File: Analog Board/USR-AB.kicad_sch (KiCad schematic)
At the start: 3 parts, among them U2 CD74HC4067SM96, U3 SC0918

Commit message: updated PDB and analog board
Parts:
- added J2, J3: S5B-XH-A_LF__SN_, USR:JST-XH 5-PIN, symbol USR:JST-XH (5-pin_RA)
- added U1: ~, USR:JST-XA 4-PIN, symbol USR:JST-XA 4-PIN
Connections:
- net LOADCELL_1 is gone; now on net M1_THERM: U2.5 (I4)
- net LOADCELL_2 is gone; now on net M2_THERM: U2.4 (I5)
- net LOADCELL_3 is gone; now on net M3_THERM: U2.3 (I6)
- net LOADCELL_4 is gone; now on net M4_THERM: U2.2 (I7)
- net AMB_THERM: now also U2.21 (I10), J2.5; no longer U2.17 (I14)
- net DRIVE1_HE: now also J1.32 (DRIVE1_HE), U2.23 (I8); no longer U2.19 (I12)
- net DRIVE2_HE: now also J1.33 (DRIVE2_HE), U2.22 (I9); no longer U2.18 (I13)
- net GND: now also U3.33 (AGND)
- net M1_THERM: now also J2.1; no longer U2.23 (I8)
- net M2_THERM: now also J2.2; no longer U2.22 (I9)
- net M3_THERM: now also J2.3; no longer U2.21 (I10)
- net M4_THERM: now also J2.4; no longer U2.20 (I11)
- net UART_RX: no longer U3.17 (GP13)
- net UART_TX: no longer U3.16 (GP12)
- net Connection_5: now reaches U2.16 (I15)
- net Connection_5: now also J3.5
- new net CLK: U1.3
- new net CS: U1.4
- new net Connection_1: J3.1, U2.20 (I11)
- new net Connection_2: J3.2, U2.19 (I12)
- new net Connection_3: J3.3, U2.18 (I13)
- new net Connection_4: J3.4, U2.17 (I14)
- new net Din: U1.1
- new net Dout: U1.2
- new net UART_RX-(host): U3.16 (GP12)
- new net UART_TX-(host): U3.17 (GP13)
- no-connect marks 3 -> 1
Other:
- note added: "(Look at PICO pinout for what these mean) SPIO SCK: CLK SPIO TX: Din SPIO RX: Dout SPIO CSn: CS"
- note added: "PDB HE sensors"
- note added: "Unused MUX connections"
- note removed: "Questions: - What analog inputs are coming in - where do we want the pico connected? - what connections on the backplane pinnout correspond to the pico on the analog board? - Pico (analog) is just connected to the UART connection on the backplane"
- note removed: "analog inputs: - load cell - load cell - load cell - load cell - LA feedback - LA feedback - LA feedback - HE sensor (PDB) - HE sensor (PDB) ... - What else?"
- note removed: "look into the analog ground for the chip"
- note removed: "use the same pin numbers for the multiplexer pins on the sheet"

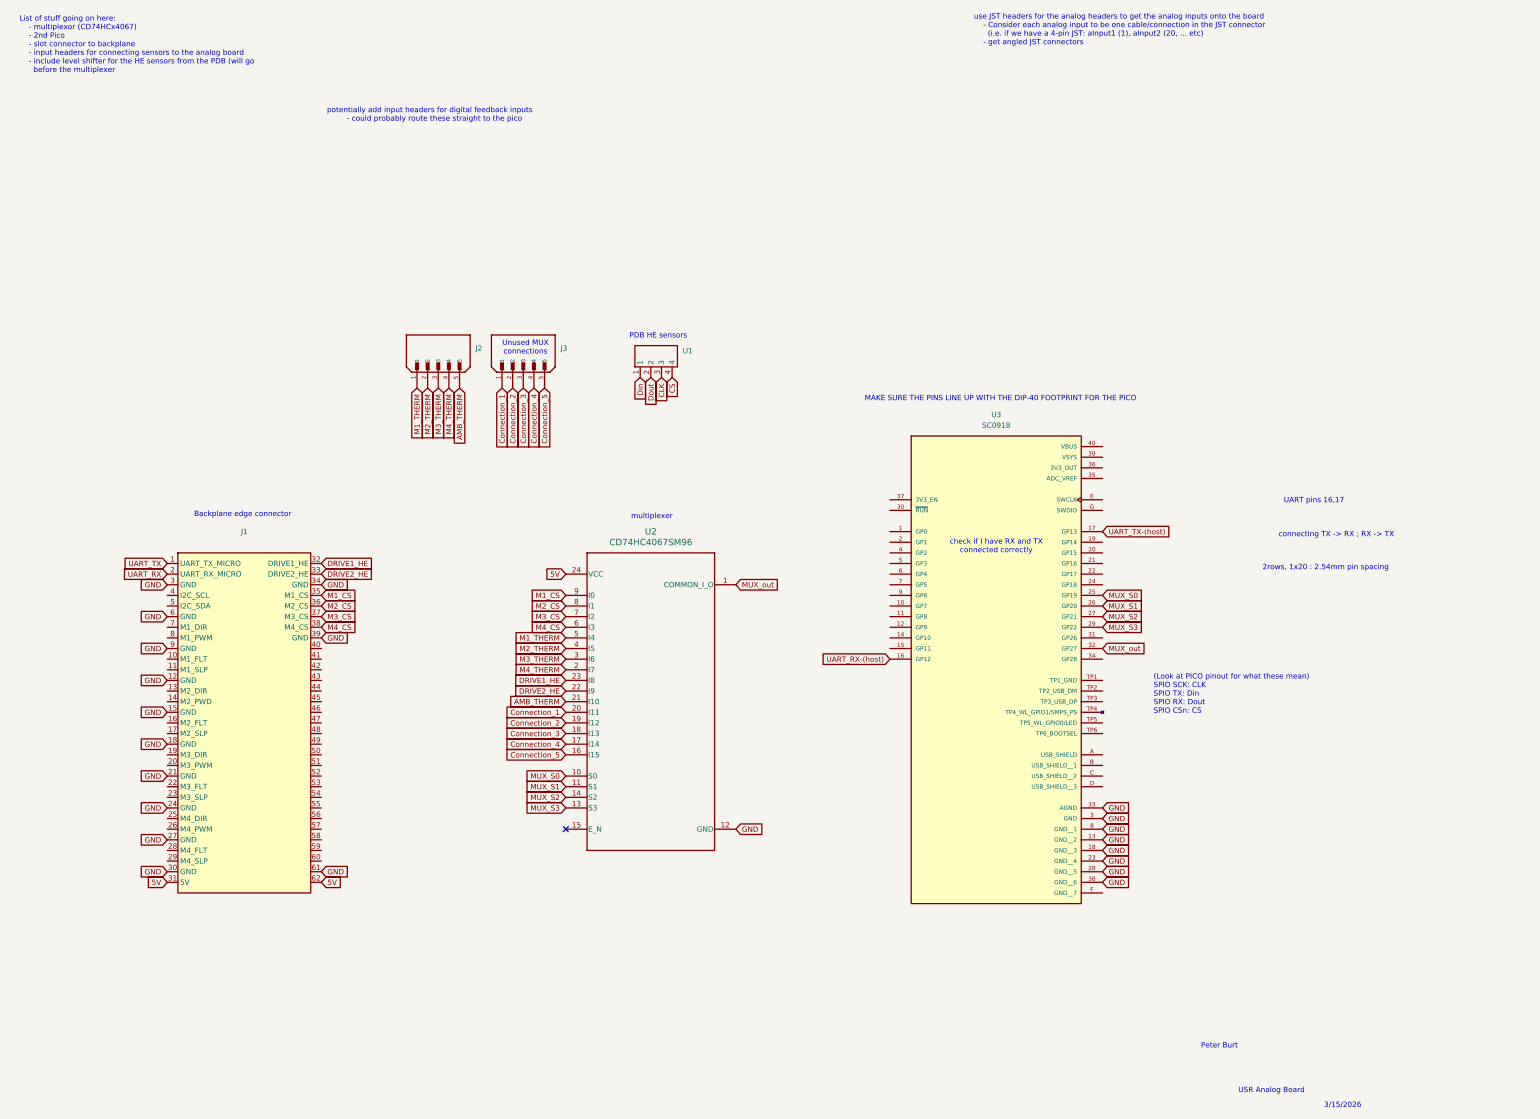
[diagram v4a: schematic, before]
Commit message: Updated analog board connections
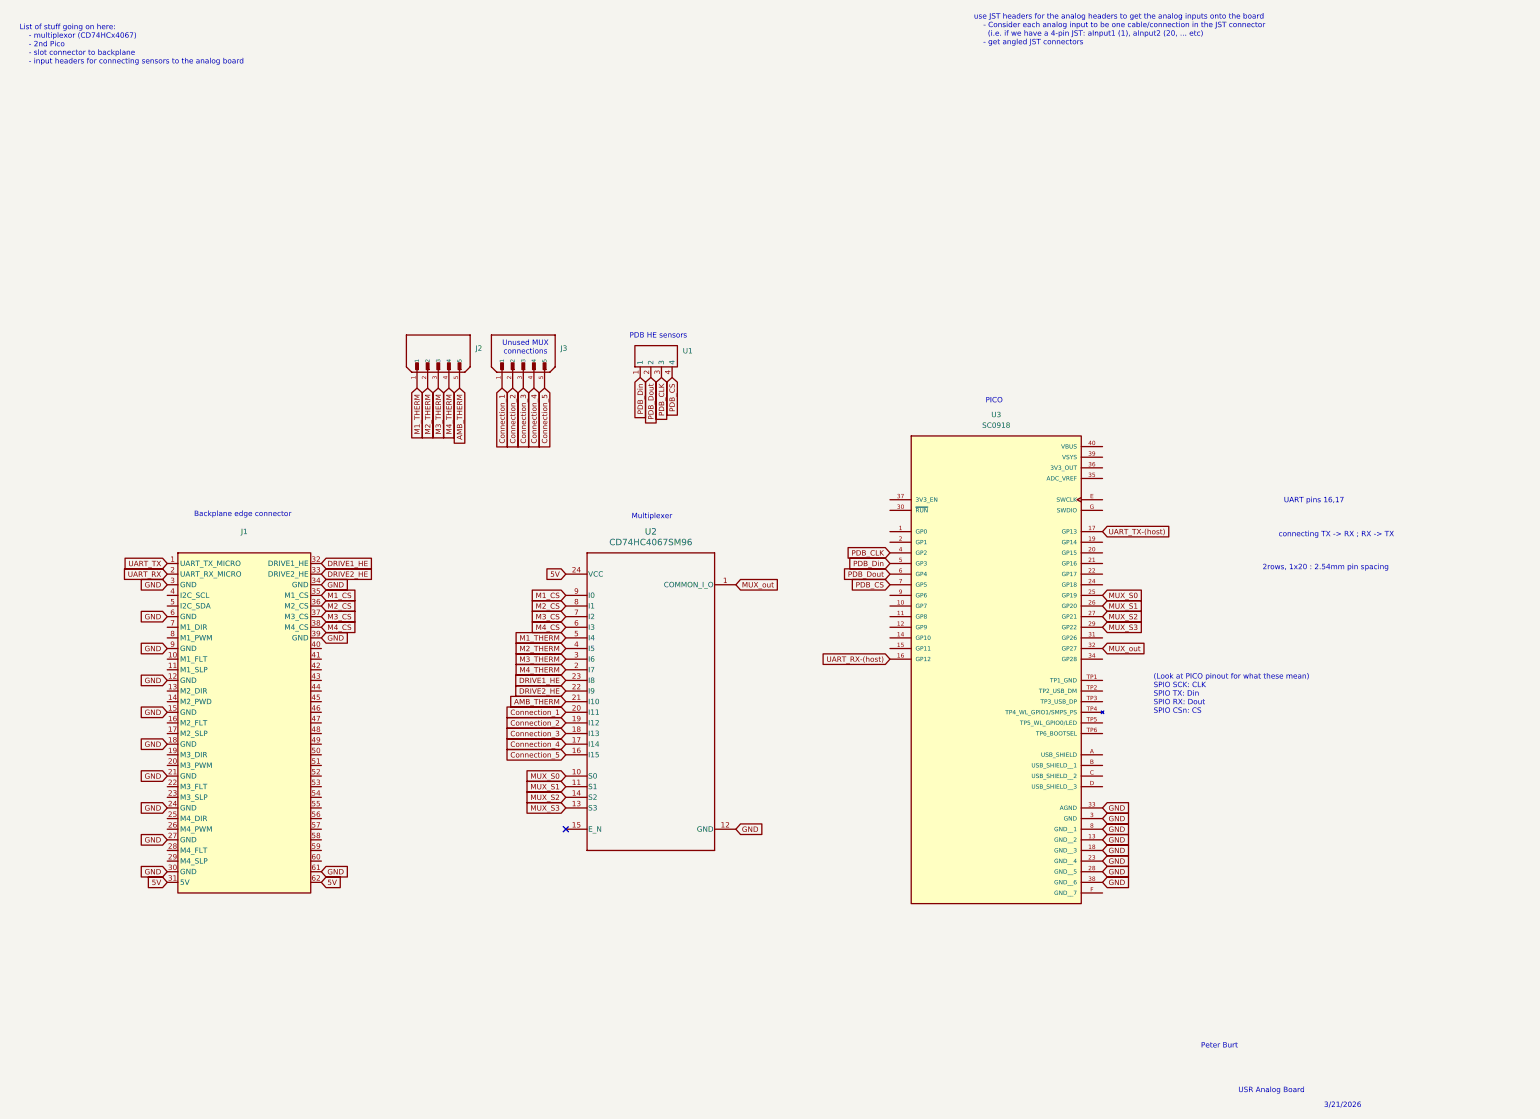
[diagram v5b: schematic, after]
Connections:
- net CLK is gone; now on net PDB_CLK: U1.3
- net CS is gone; now on net PDB_CS: U1.4
- net Din is gone; now on net PDB_Din: U1.1
- net Dout is gone; now on net PDB_Dout: U1.2
- net PDB_CLK: now reaches U3.4 (GP2)
- net PDB_Din: now reaches U3.5 (GP3)
- net PDB_Dout: now reaches U3.6 (GP4)
- net PDB_CS: now reaches U3.7 (GP5)
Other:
- note added: "3/21/2026"
- note added: "List of stuff going on here: - multiplexor (CD74HCx4067) - 2nd Pico - slot connector to backplane - input headers for connecting sensors to the analog board"
- note added: "Multiplexer"
- note added: "PICO"
- note removed: "3/15/2026"
- note removed: "List of stuff going on here: - multiplexor (CD74HCx4067) - 2nd Pico - slot connector to backplane - input headers for connecting sensors to the analog board - include level shifter for the HE sensors from the PDB (will go before the multiplexer"
- note removed: "MAKE SURE THE PINS LINE UP WITH THE DIP-40 FOOTPRINT FOR THE PICO"
- note removed: "check if I have RX and TX connected correctly"
- note removed: "multiplexer"
- note removed: "potentially add input headers for digital feedback inputs - could probably route these straight to the pico"
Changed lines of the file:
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@@
+		)
+	)
+	(text "PICO"
+		(exclude_from_sim no)
+		(at 252.222 112.268 0)
+		(effects
+			(font
+				(size 1.27 1.27)
+			)
 		)
 	)
@@
 		)
 	)
-	(text "List of stuff going on here:\n	- multiplexor (CD74HCx4067)	\n	- 2nd Pico\n	- slot connector to backplane	\n	- input headers for connecting sensors to the analog board\n	- include level shifter for the HE sensors from the PDB (will go \n	  before the multiplexer"
+	(text "List of stuff going on here:\n	- multiplexor (CD74HCx4067)	\n	- 2nd Pico\n	- slot connector to backplane	\n	- input headers for connecting sensors to the analog board"
 		(exclude_from_sim no)
 		(at 19.304 27.178 0)
@@
 		)
 	)
-	(text "potentially add input headers for digital feedback inputs \n	- could probably route these straight to the pico"
-		(exclude_from_sim no)
-		(at 117.348 43.942 0)
-		(effects
-			(font
-				(size 1.27 1.27)
-			)
-		)
-	)
 	(text "Unused MUX \nconnections"
 		(exclude_from_sim no)
@@
 		)
 	)
-	(text "3/15/2026"
+	(text "3/21/2026"
 		(exclude_from_sim no)
 		(at 335.534 280.67 0)
@@
 		)
 	)
-	(text "check if I have RX and TX\nconnected correctly"
-		(exclude_from_sim no)
-		(at 252.73 147.066 0)
-		(effects
-			(font
-				(size 1.27 1.27)
-			)
-		)
-	)
-	(text "multiplexer\n"
+	(text "Multiplexer\n"
 		(exclude_from_sim no)
 		(at 170.434 139.954 0)
@@
 		)
 	)
-	(text "MAKE SURE THE PINS LINE UP WITH THE DIP-40 FOOTPRINT FOR THE PICO"
-		(exclude_from_sim no)
-		(at 253.746 111.76 0)
-		(effects
-			(font
-				(size 1.27 1.27)
-			)
-		)
-	)
 	(no_connect
 		(at 149.86 214.63)
@@
 		)
 	)
+	(global_label "PDB_Dout"
+		(shape input)
+		(at 227.33 153.67 180)
+		(fields_autoplaced yes)
+		(effects
+			(font
+				(size 1.27 1.27)
+			)
+			(justify right)
+		)
+		(property "Intersheetrefs" "${INTERSHEET_REFS}"
+			(at 215.2735 153.67 0)
+			(effects
+				(font
+					(size 1.27 1.27)
+				)
+				(justify right)
+				(hide yes)
+			)
+		)
+	)
 	(global_label "MUX_S1"
 		(shape input)
@@
 		)
 	)
-	(global_label "Din"
+	(global_label "PDB_Din"
 		(shape input)
 		(at 167.64 106.68 270)
@@
 		)
 		(property "Intersheetrefs" "${INTERSHEET_REFS}"
-			(at 167.64 112.689 90)
+			(at 167.64 117.4666 90)
 			(effects
 				(font
@@
 		)
 	)
-	(global_label "CLK"
+	(global_label "PDB_CLK"
 		(shape input)
 		(at 172.72 106.68 270)
@@
 		)
 		(property "Intersheetrefs" "${INTERSHEET_REFS}"
-			(at 172.72 113.2333 90)
+			(at 172.72 118.0109 90)
 			(effects
 				(font
@@
 		)
 	)
+	(global_label "PDB_CLK"
+		(shape input)
+		(at 227.33 148.59 180)
+		(fields_autoplaced yes)
+		(effects
+			(font
+				(size 1.27 1.27)
+			)
+			(justify right)
+		)
+		(property "Intersheetrefs" "${INTERSHEET_REFS}"
+			(at 215.9991 148.59 0)
+			(effects
+				(font
+					(size 1.27 1.27)
+				)
+				(justify right)
+				(hide yes)
+			)
+		)
+	)
 	(global_label "MUX_out"
 		(shape input)
@@
 		)
 	)
+	(global_label "PDB_Din"
+		(shape input)
+		(at 227.33 151.13 180)
+		(fields_autoplaced yes)
+		(effects
+			(font
+				(size 1.27 1.27)
+			)
+			(justify right)
+		)
+		(property "Intersheetrefs" "${INTERSHEET_REFS}"
+			(at 216.5434 151.13 0)
+			(effects
+				(font
+					(size 1.27 1.27)
+				)
+				(justify right)
+				(hide yes)
+			)
+		)
+	)
 	(global_label "GND"
 		(shape input)
@@
 		)
 	)
-	(global_label "Dout"
+	(global_label "PDB_Dout"
 		(shape input)
 		(at 170.18 106.68 270)
@@
 		)
 		(property "Intersheetrefs" "${INTERSHEET_REFS}"
-			(at 170.18 113.9589 90)
+			(at 170.18 118.7365 90)
 			(effects
 				(font
@@
 		)
 	)
+	(global_label "PDB_CS"
+		(shape input)
+		(at 227.33 156.21 180)
+		(fields_autoplaced yes)
+		(effects
+			(font
+				(size 1.27 1.27)
+			)
+			(justify right)
+		)
+		(property "Intersheetrefs" "${INTERSHEET_REFS}"
+			(at 217.0877 156.21 0)
+			(effects
+				(font
+					(size 1.27 1.27)
+				)
+				(justify right)
+				(hide yes)
+			)
+		)
+	)
 	(global_label "Connection_1"
 		(shape input)
@@
 		)
 	)
-	(global_label "CS"
+	(global_label "PDB_CS"
 		(shape input)
 		(at 175.26 106.68 270)
@@
 		)
 		(property "Intersheetrefs" "${INTERSHEET_REFS}"
-			(at 175.26 112.1447 90)
-			(effects
-				(font
+			(at 175.26 116.9223 90)
+			(effects
+				(font

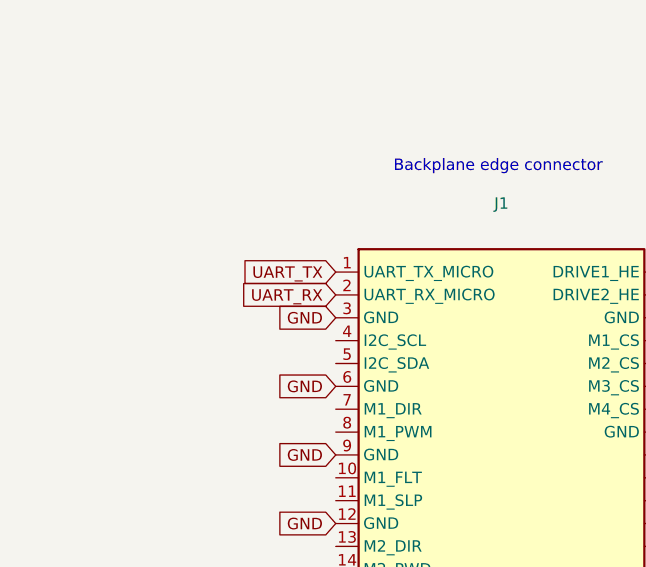
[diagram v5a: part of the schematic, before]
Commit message: Finished Analog board PCB
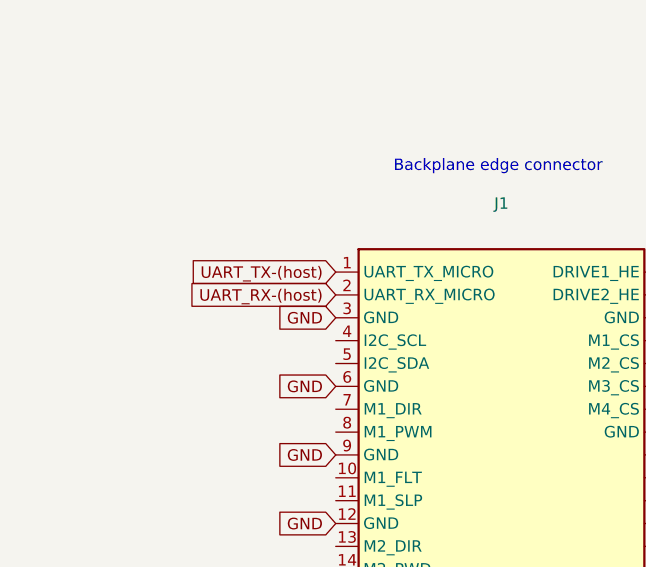
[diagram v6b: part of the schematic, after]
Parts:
- J1: value ~ -> (none); footprint USR:USR-62P-SLOT -> USR:BUS_XT
- U1: value ~ -> (none)
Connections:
- net UART_RX is gone; now on net UART_RX-(host): J1.2 (UART_RX_MICRO)
- net UART_TX is gone; now on net UART_TX-(host): J1.1 (UART_TX_MICRO)

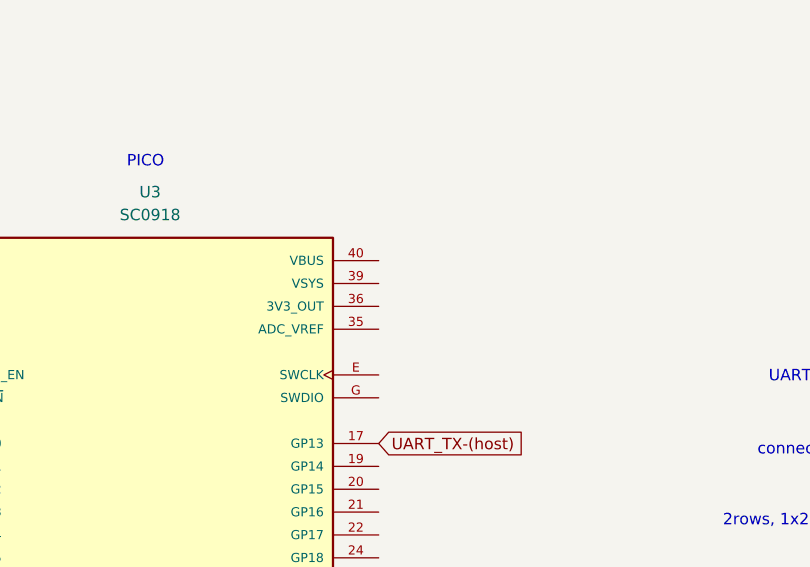
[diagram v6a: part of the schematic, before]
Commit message: [Analog Board] added power to PICO, updated board dimensions
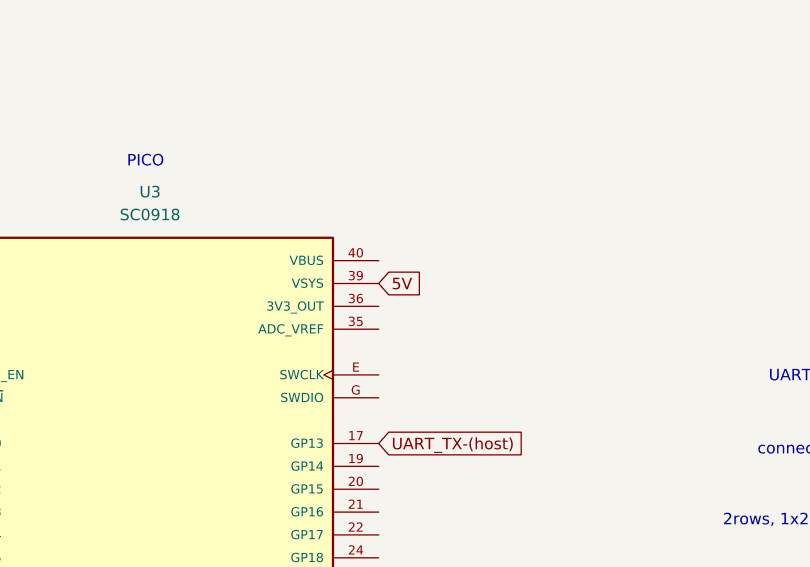
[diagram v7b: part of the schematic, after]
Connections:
- net 5V: now also U3.39 (VSYS)
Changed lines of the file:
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@@
+		)
+	)
+	(global_label "5V"
+		(shape input)
+		(at 278.13 125.73 0)
+		(fields_autoplaced yes)
+		(effects
+			(font
+				(size 1.27 1.27)
+			)
+			(justify left)
+		)
+		(property "Intersheetrefs" "${INTERSHEET_REFS}"
+			(at 283.4133 125.73 0)
+			(hide yes)
+			(show_name no)
+			(do_not_autoplace no)
+			(effects
+				(font
+					(size 1.27 1.27)
+				)
+				(justify left)
+			)
 		)
 	)
